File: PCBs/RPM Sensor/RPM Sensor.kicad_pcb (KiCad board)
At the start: 2 copper layers, 39.4 x 40 mm, 23 parts, among them J1 I, J10 DO/DO, J11 SEL/SEL, J12 I, J13 I, J14 I, J15 I, J16 I, J2 B, J3 I, J4 A, J5 U, J6 V, J7 W/PWM, J8 SCL/CLK, J9 NSL/DI, U1 MAG_ENCODER_AEAT-8800-Q24

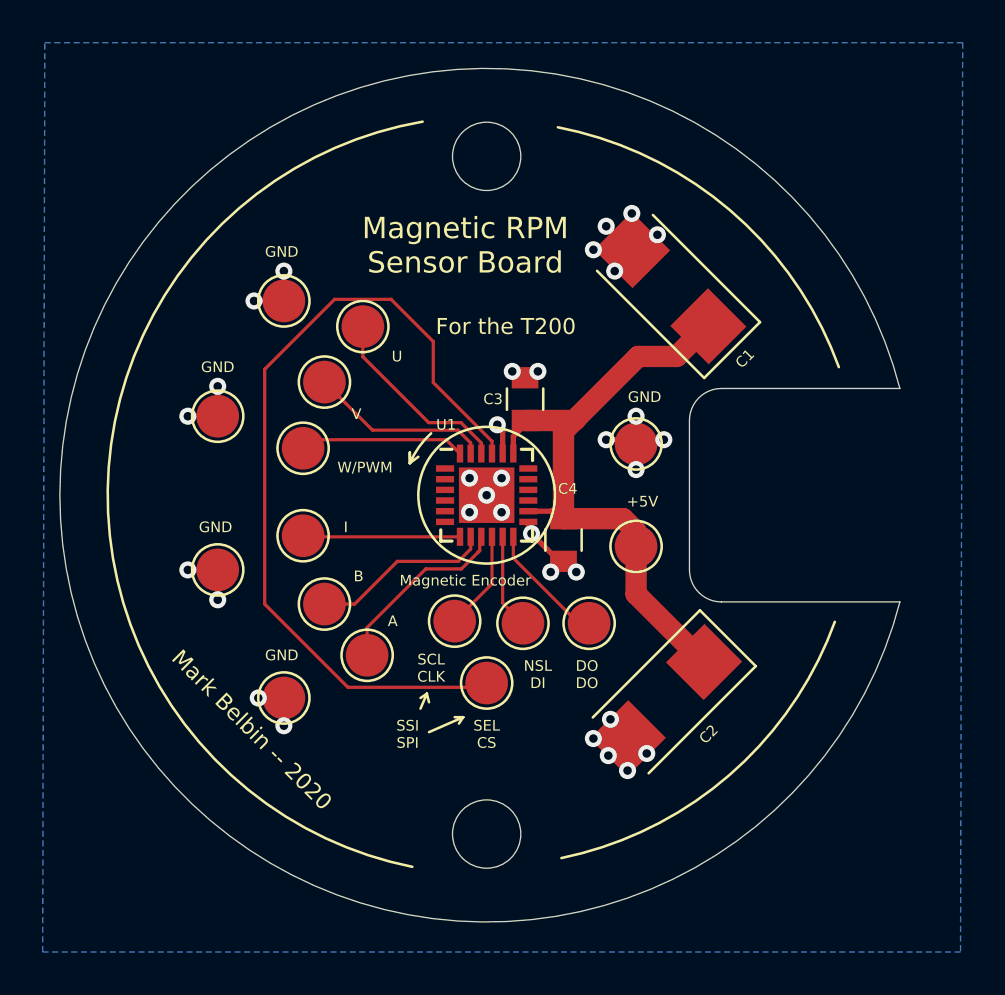
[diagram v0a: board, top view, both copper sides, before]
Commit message: Fixed Footprint and Gerbers
- Changed mag encoder from 4x4 to 5x5, the correct footprint. :(
- Updated Gerbers
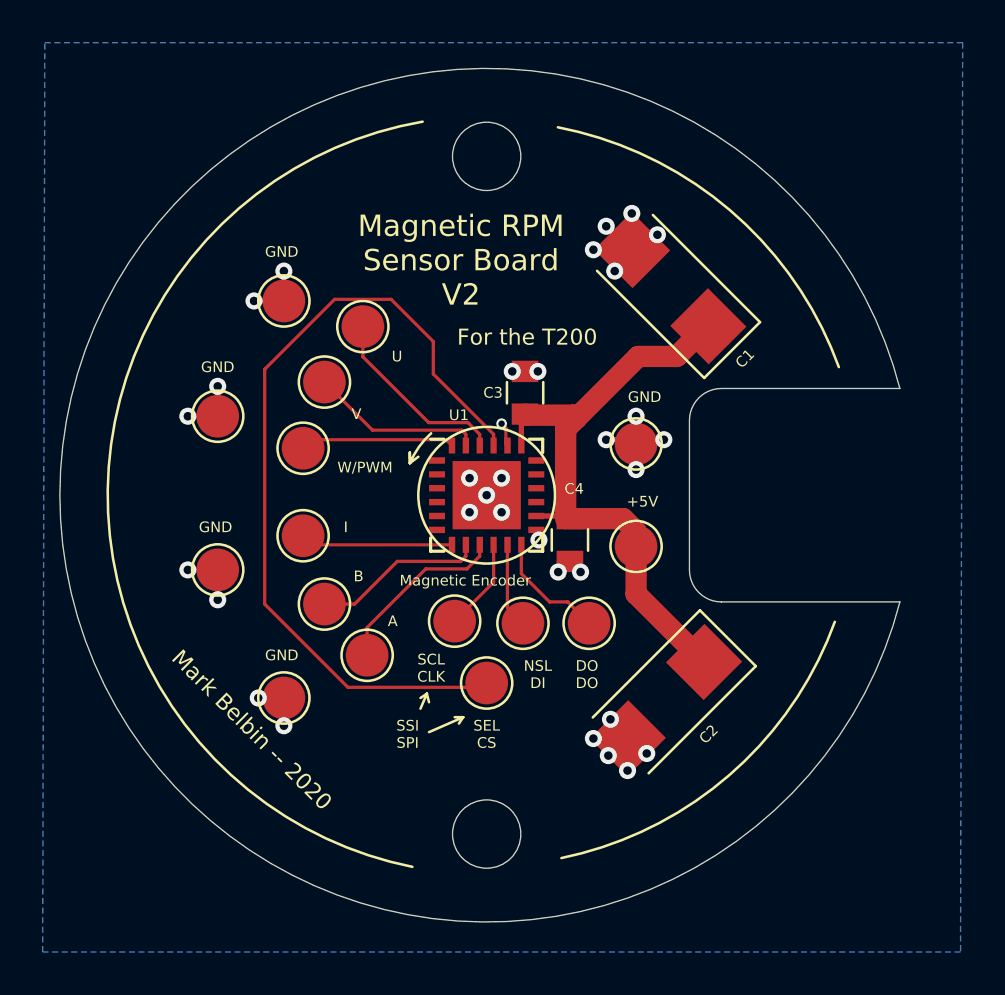
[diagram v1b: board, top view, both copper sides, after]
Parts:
- U1: footprint Housings_DFN_QFN:QFN-24-1EP_4x4mm_Pitch0.5mm -> Housings_DFN_QFN:QFN-24-1EP_5x5mm_Pitch0.65mm
- moved C4 0.30 mm to (103.9, 102.1)
- moved C3 0.30 mm to (101.8, 95.2)
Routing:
- net GND: track 22.3 -> 19.8 mm
- net +5V: track 30.3 -> 28.7 mm
- net Net-(J7-Pad1): track 7.78 -> 7.25 mm
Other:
- board text added: "Magnetic RPM Sensor Board V2"
